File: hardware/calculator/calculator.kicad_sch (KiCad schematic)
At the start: 6 parts, among them U1 WeMos_D1_mini, U2 MPR121QR2, U3 MPR121QR2, U4 MAX7219, U5 TXB0104D

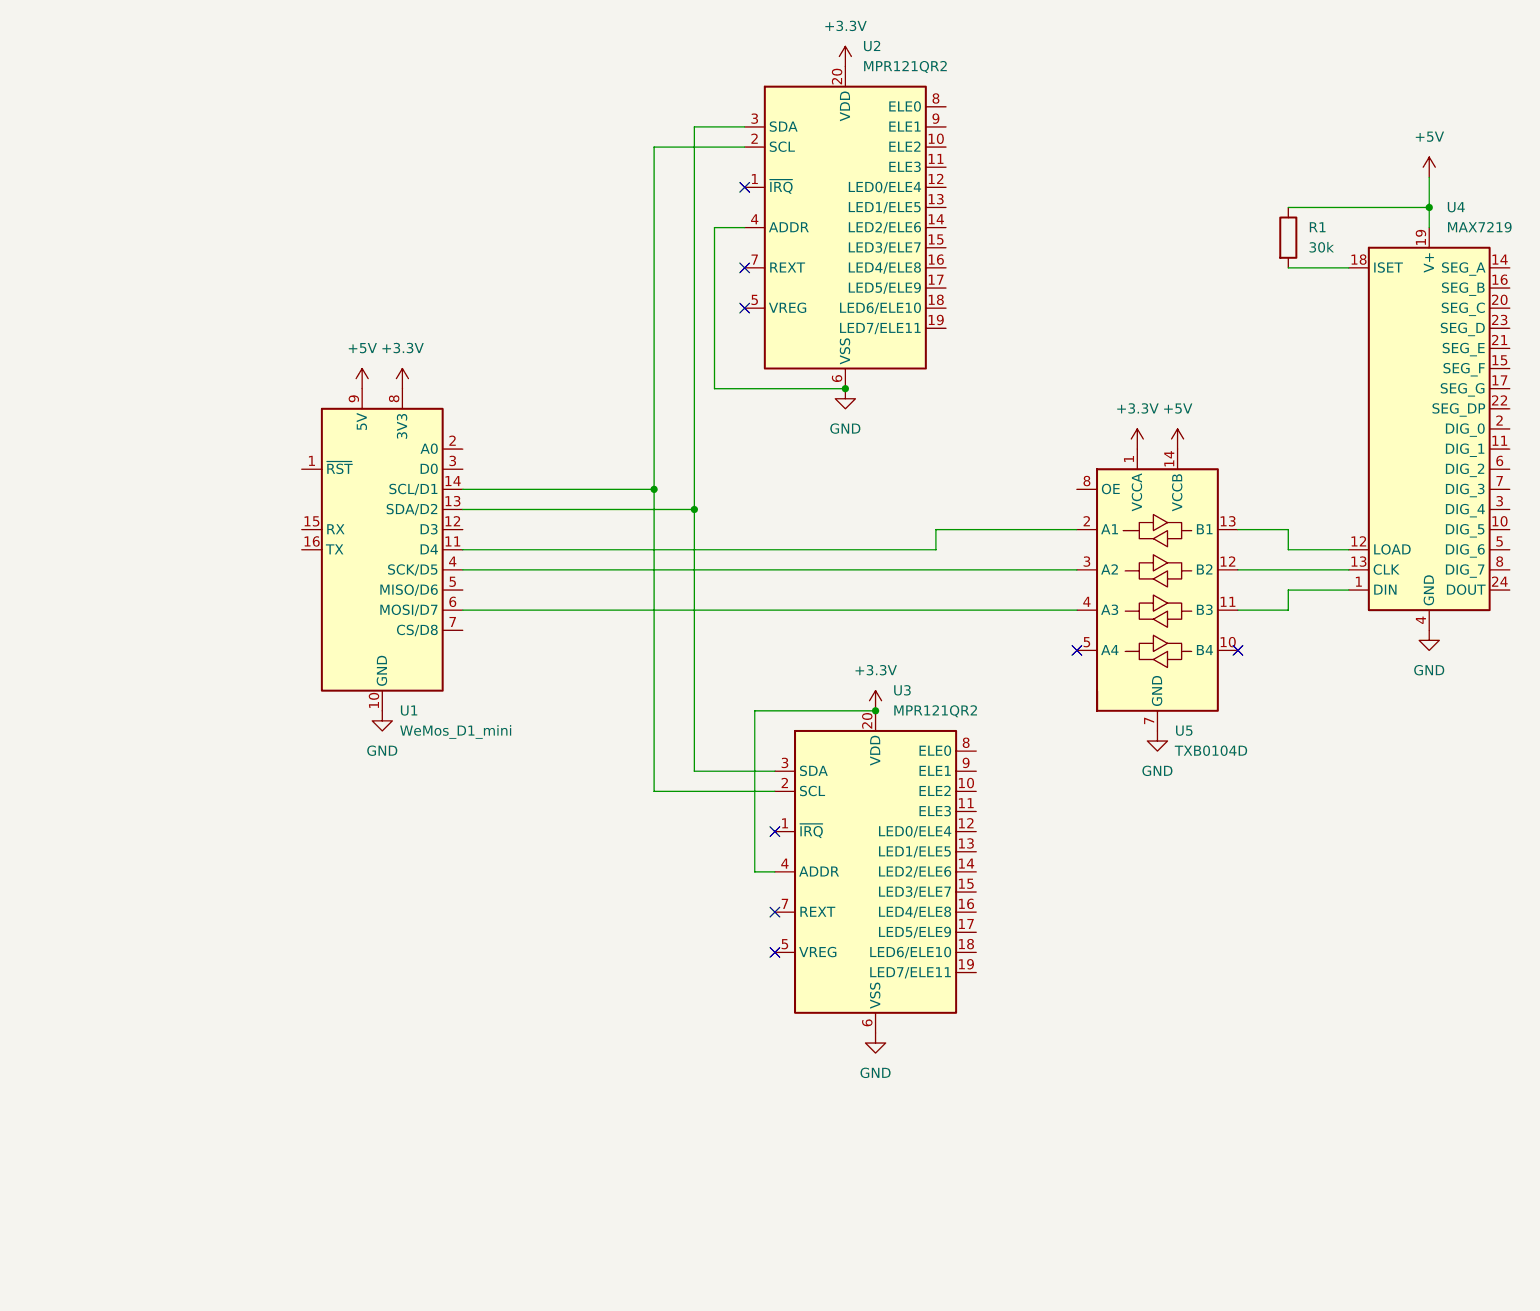
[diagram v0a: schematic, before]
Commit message: Added display pcb
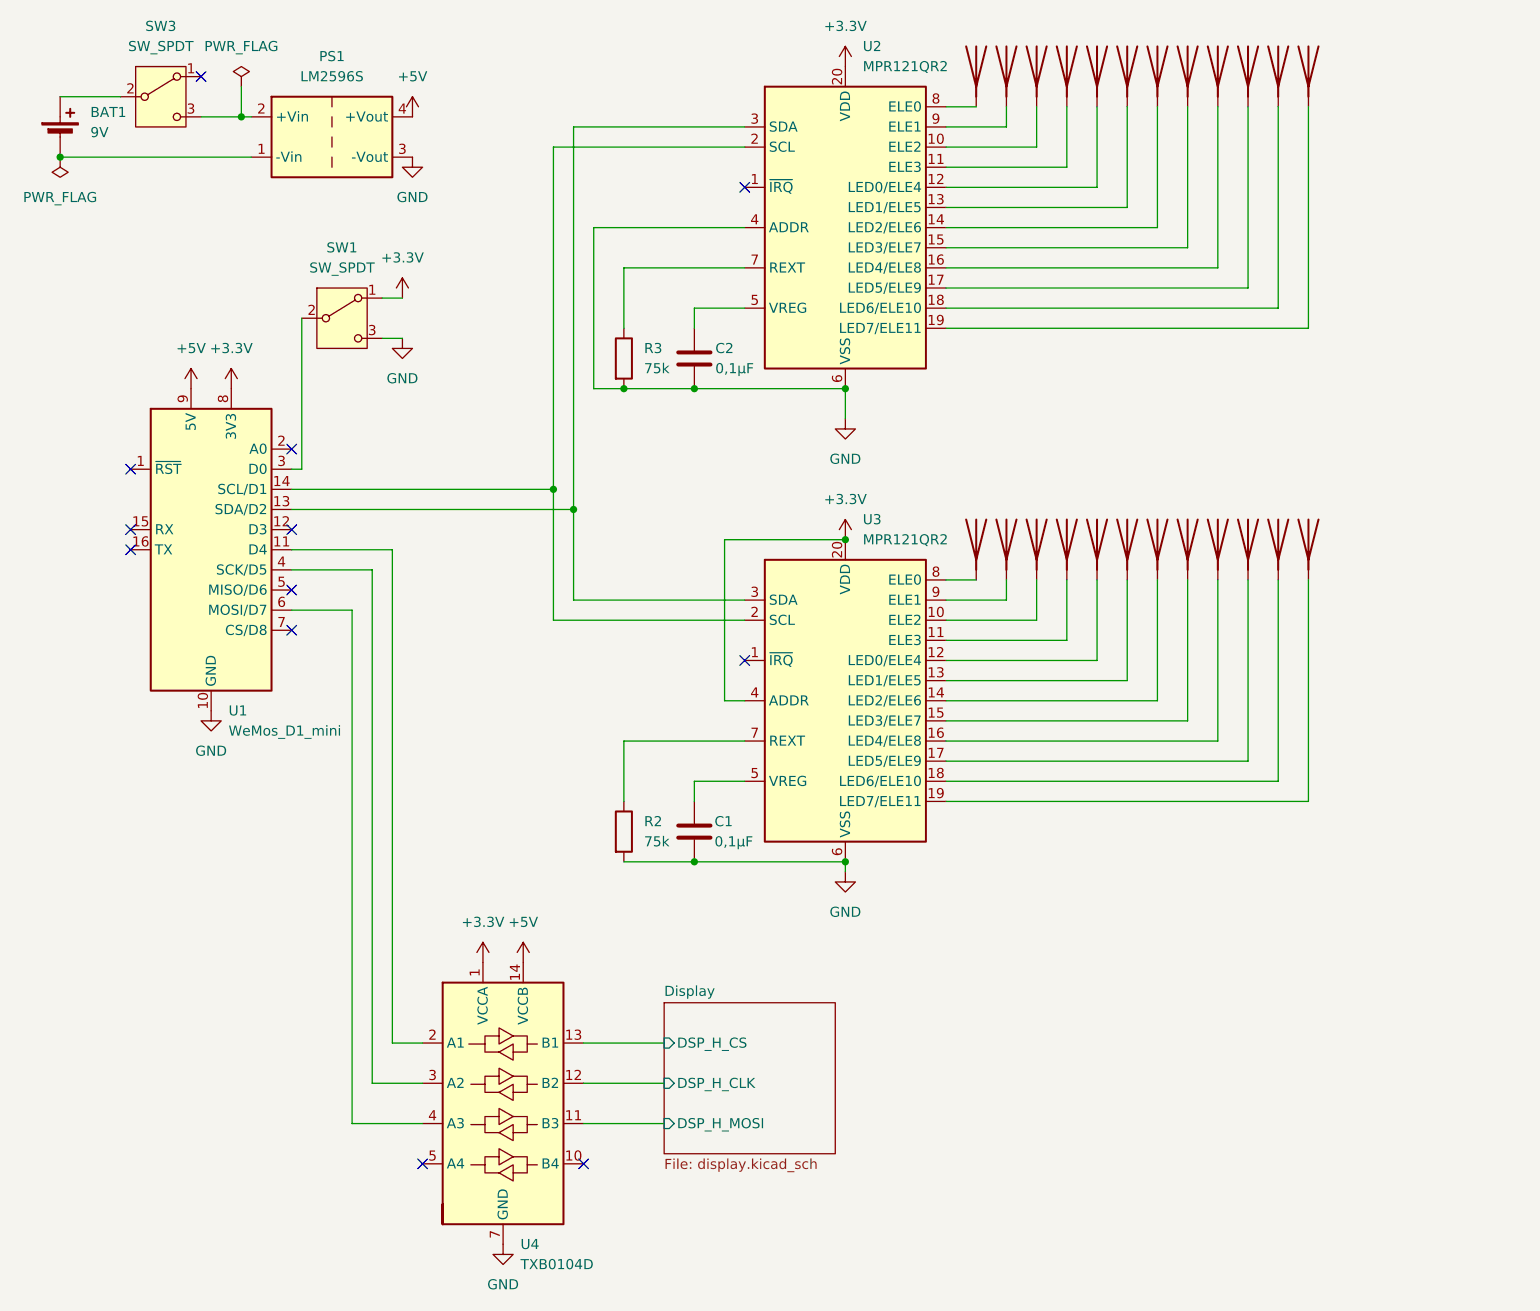
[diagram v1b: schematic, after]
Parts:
- removed R1: 30k, symbol Device:R
- removed U4: MAX7219, symbol Driver_LED:MAX7219
- removed U5: TXB0104D, Package_SO:SOIC-14_3.9x8.7mm_P1.27mm, symbol Logic_LevelTranslator:TXB0104D
- added BAT1: 9V, symbol Device:Battery_Cell
- added BT1, BT10, BT11, BT12, BT13, BT14, BT15, BT16, BT17, BT18, BT19, BT2, BT20, BT21, BT22, BT23, BT24, BT3, BT4, BT5, BT6, BT7, BT8, BT9: Antenna, symbol Device:Antenna
- added C1, C2: 0,1µF, symbol Device:C
- added PS1: LM2596S, Converter_DCDC:Converter_DCDC_Murata_MEE1SxxxxSC_THT, symbol Converter_DCDC:MEE1S1505SC
- added R2, R3: 75k, symbol Device:R
- added SW1, SW3: SW_SPDT, symbol Switch:SW_SPDT
- added U4: TXB0104D, Package_SO:SOIC-14_3.9x8.7mm_P1.27mm, symbol Logic_LevelTranslator:TXB0104D
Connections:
- net +3.3V: now also SW1.1 (A), U4.1 (VCCA)
- net +5V: now also PS1.4 (+Vout), U4.14 (VCCB)
- net GND: now also C1.2, C2.2, PS1.3 (-Vout), R2.2, R3.2, SW1.3 (C), U4.7 (GND)
- net at U1.11 (D4): now also U4.2 (A1)
- net at U1.4 (SCK/D5): now also U4.3 (A2)
- net at U1.6 (MOSI/D7): now also U4.4 (A3)
- net at U3.10 (ELE2): now also BT15.1 (A)
- net at U3.11 (ELE3): now also BT16.1 (A)
- net at U3.12 (LED0/ELE4): now also BT17.1 (A)
- net at U3.13 (LED1/ELE5): now also BT18.1 (A)
- net at U3.14 (LED2/ELE6): now also BT19.1 (A)
- net at U3.15 (LED3/ELE7): now also BT20.1 (A)
- net at U3.16 (LED4/ELE8): now also BT21.1 (A)
- net at U3.17 (LED5/ELE9): now also BT22.1 (A)
- net at U3.18 (LED6/ELE10): now also BT23.1 (A)
- net at U3.19 (LED7/ELE11): now also BT24.1 (A)
- net at U3.5 (VREG): now also C1.1
- net at U3.7 (REXT): now also R2.1
- net at U3.8 (ELE0): now also BT13.1 (A)
- net at U3.9 (ELE1): now also BT14.1 (A)
- net at U2.10 (ELE2): now also BT3.1 (A)
- net at U2.11 (ELE3): now also BT4.1 (A)
- net at U2.12 (LED0/ELE4): now also BT5.1 (A)
- net at U2.13 (LED1/ELE5): now also BT6.1 (A)
- net at U2.14 (LED2/ELE6): now also BT7.1 (A)
- net at U2.15 (LED3/ELE7): now also BT8.1 (A)
- net at U2.16 (LED4/ELE8): now also BT9.1 (A)
- net at U2.17 (LED5/ELE9): now also BT10.1 (A)
- net at U2.18 (LED6/ELE10): now also BT11.1 (A)
- net at U2.19 (LED7/ELE11): now also BT12.1 (A)
- net at U2.5 (VREG): now also C2.1
- net at U2.7 (REXT): now also R3.1
- net at U2.8 (ELE0): now also BT1.1 (A)
- net at U2.9 (ELE1): now also BT2.1 (A)
- net at U1.3 (D0): now also SW1.2 (B)
- new net: BAT1.1 (+), SW3.2 (B)
- new net: PS1.2 (+Vin), SW3.3 (C)
- new net: BAT1.2 (-), PS1.1 (-Vin)
- new net Display/DSP_H_CLK: U4.12 (B2)
- new net Display/DSP_H_CS: U4.13 (B1)
- new net Display/DSP_H_MOSI: U4.11 (B3)
- no-connect marks 8 -> 12
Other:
- added sheet Display (display.kicad_sch)
- moved on the sheet: U1, U3
